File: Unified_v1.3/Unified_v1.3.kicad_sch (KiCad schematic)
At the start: 1 part

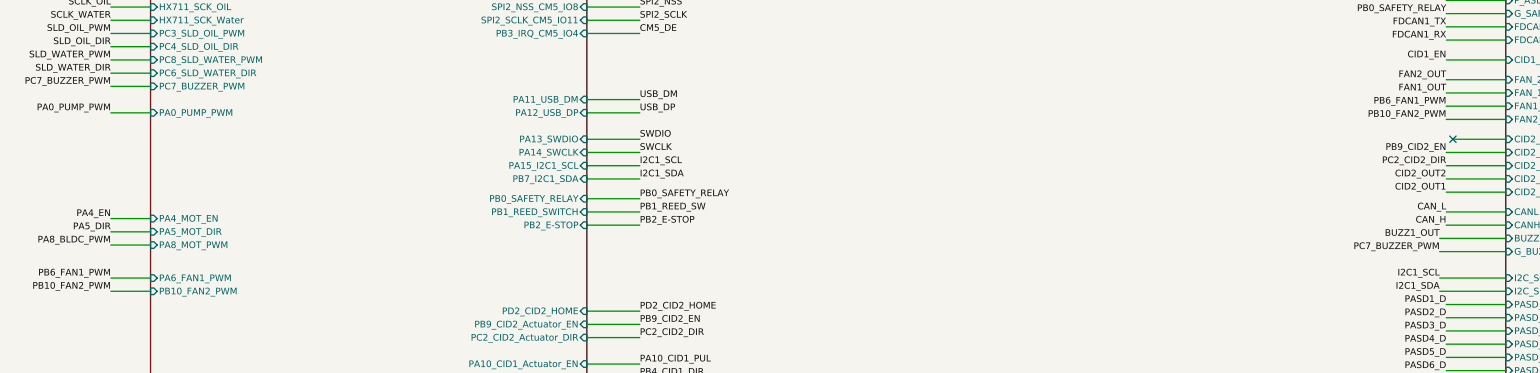
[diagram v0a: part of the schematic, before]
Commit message: fix: correct feedback dividers, net label, and TEMP pin circuit
- C-01: R36 71.5K → 14K (U8 MP1584EN Vout: 1.92V → 6.51V target 6.5V)
- C-05: R26 37.4K → 52.3K (U5 TPS54531 Vout: 3.79V → 4.98V target 5V)
- H-01: Rename root label PB6_FAN1_PWM → PA6_FAN1_PWM (was wrong pin ref)
- H-06: Add R92 (100K) between TP4056 TEMP pin and GND (was shorted to
  PROG/GND junction, bypassing thermal protection entirely)

Co-Authored-By: Claude Opus 4.6 (1M context) <noreply@anthropic.com>
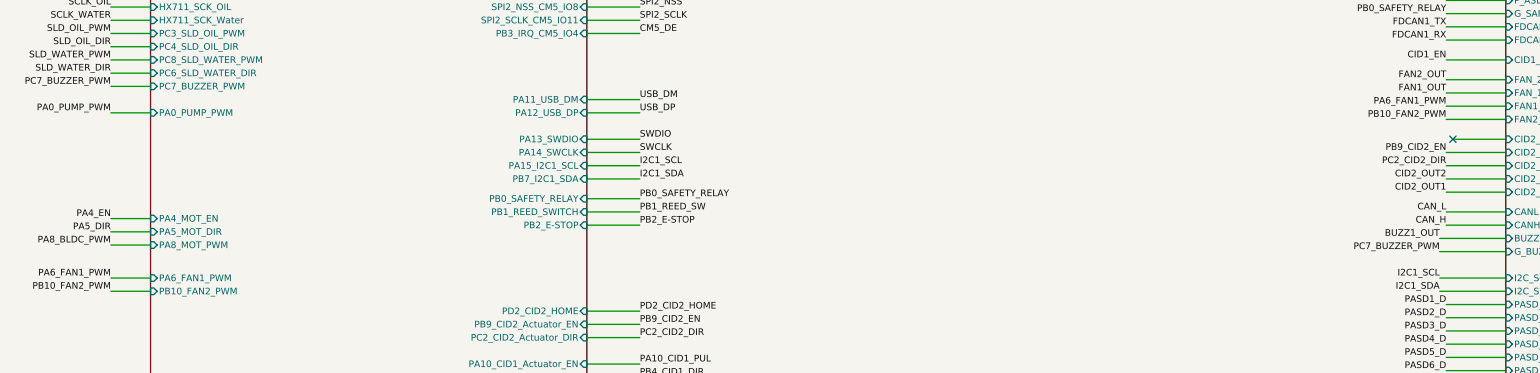
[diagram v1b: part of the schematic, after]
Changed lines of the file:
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@@
 		)
 	)
-	(label "PB6_FAN1_PWM"
+	(label "PA6_FAN1_PWM"
 		(at 30.48 97.79 180)
 		(effects
@@
 		)
 	)
-	(label "PB6_FAN1_PWM"
+	(label "PA6_FAN1_PWM"
 		(at 287.02 64.77 180)
 		(effects
